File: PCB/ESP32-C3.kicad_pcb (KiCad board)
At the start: 2 copper layers, 28.3 x 28.5 mm, 50 parts, among them J1 HCZZ0039-3, J2 DPS_PPS_Right_Angle, SW1 TS-1187A-B-A-B, SW2 TS-1187A-B-A-B, U1 USB-C-16P-SMD, U2 BQ24073RGTR, U3 ESP32-C3, U4 DS8242-33SS3, Y1 40MHz_S3240000151040

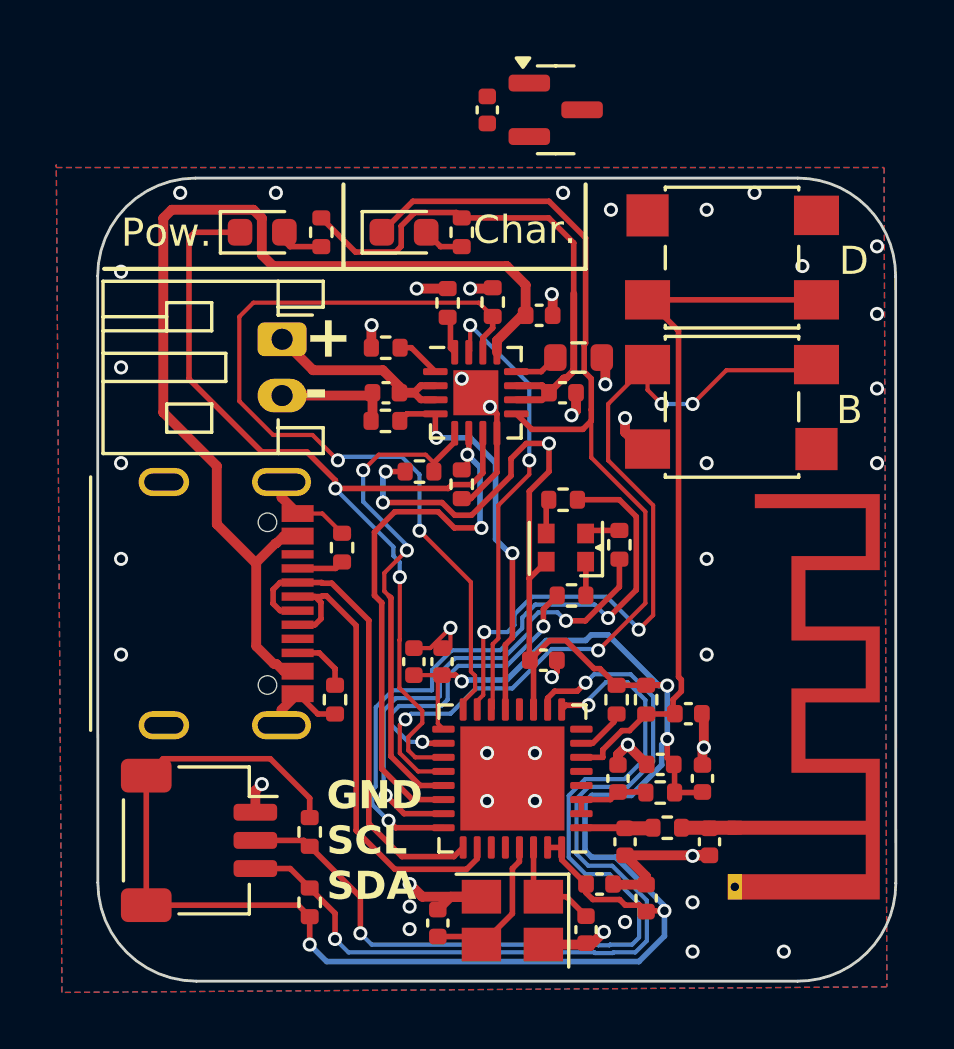
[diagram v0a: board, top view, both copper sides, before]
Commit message: LDO hinzugefügt
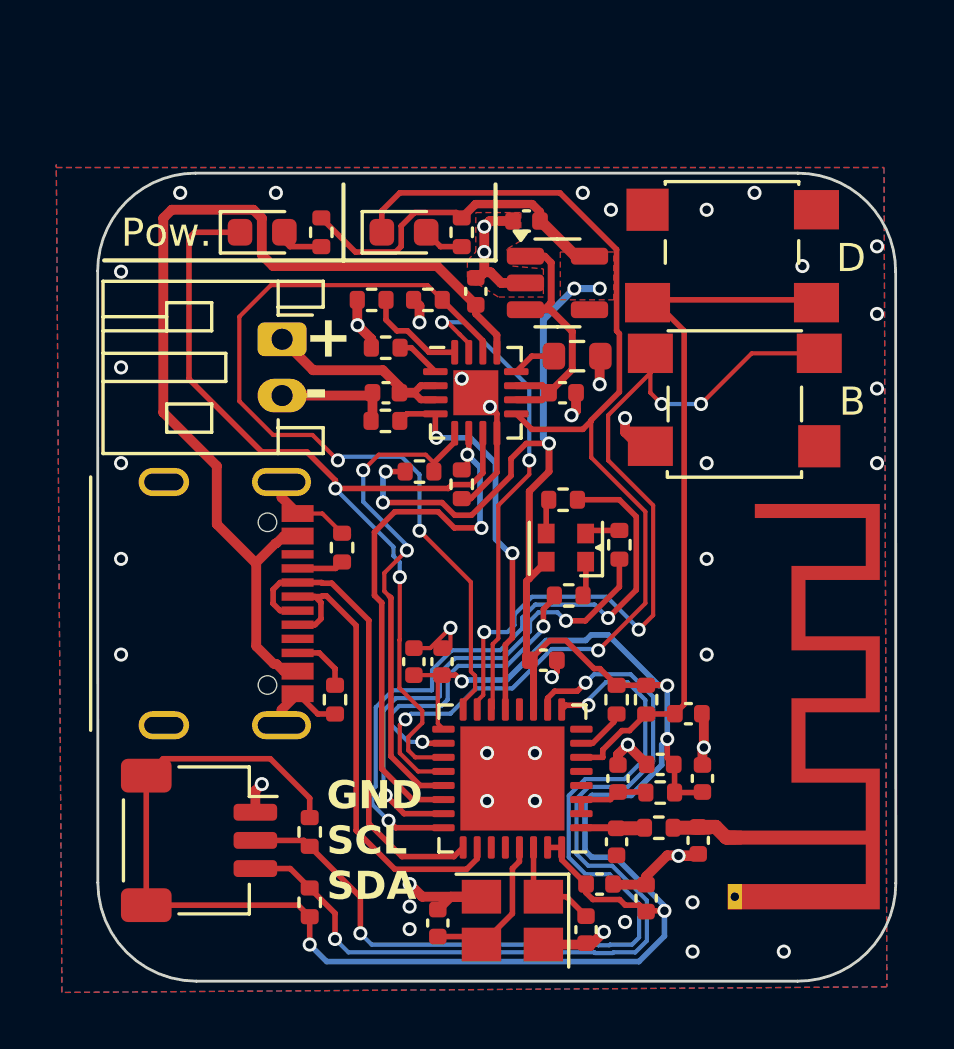
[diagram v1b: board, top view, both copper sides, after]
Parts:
- removed R19, R21: 100_0402, Resistor_SMD:R_0402_1005Metric
- removed U4: DS8242-33SS3, Package_TO_SOT_SMD:SOT-23
- added R12: 120_0402, Resistor_SMD:R_0402_1005Metric, F.Cu at (145.7, 82.6)
- added R13: 120_0402, Resistor_SMD:R_0402_1005Metric, F.Cu at (145.5, 79.2)
- added U5: WL9003S5-33, Package_TO_SOT_SMD:SOT-23-5, F.Cu at (145.3, 71.5)
- R14: value 100_0402 -> 120_0402
- moved C9 4.18 mm to (144.2, 69.3), turned to 180 degrees
- moved R18 2.70 mm to (138.7, 72.1), turned to 180 degrees
- moved R14 2.56 mm to (147.5, 80.8), turned to 90 degrees
- moved C19 2.41 mm to (142.4, 71.8), turned to 90 degrees
- moved R5 2.30 mm to (140.7, 72.1), turned to 0 degrees
- moved C3 0.40 mm to (150.3, 91.3)
- moved AE1 0.35 mm to (151.6, 91.2)
- moved C6 0.30 mm to (147.4, 91.3)
- moved L1 0.30 mm to (148.9, 90.8)
- moved SW1 0.20 mm to (151.5, 70.4)
- moved SW2 0.14 mm to (151.6, 75.8)
- moved R15 0.07 mm to (146.0, 74.1)
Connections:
- R14 pad 1: Grün -> Blau
- R14 pad 2: Net-(D1-GK) -> Net-(D1-BK)
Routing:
- net Net-(U5-EN): track 0.00 -> 10.3 mm
- net GND: track 42.8 -> 45.5 mm
- net VCC: track 38.1 -> 35.6 mm
- net Net-(U2-ISET): track 1.35 -> 3.63 mm
- net TD: track 16.1 -> 17.6 mm
- net NCHG: track 38.9 -> 40.4 mm
- net Net-(U3-GPIO9): track 27.9 -> 29.0 mm
- net Net-(AE1-A): track 1.91 -> 2.66 mm
- net Net-(U3-LNA_IN): track 2.56 -> 1.96 mm
- net +3.3V: track 111.4 -> 111.5 mm, vias 8 -> 10
- added copper zone on F.Cu, net +3.3V
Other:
- board size 28.3 x 28.5 mm -> 28.3 x 28.7 mm
- board text removed: "Char."

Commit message: Kleine Verbesserungen
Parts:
- D1: footprint LEDSMD:LED_0606_1432 -> LEDSMD:LED_0606_1432_correct
- turned D1 to 0 degrees
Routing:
- net Net-(D1-RK): track 1.20 -> 2.74 mm
- net Net-(D1-GK): track 1.24 -> 2.09 mm
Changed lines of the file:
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@@
 		)
 	)
-	(footprint "LEDSMD:LED_0606_1432"
+	(footprint "LEDSMD:LED_0606_1432_correct"
 		(layer "F.Cu")
-		(at 145.6 80.9 180)
+		(at 145.6 80.9)
 		(property "Reference" "D1"
-			(at 1.6 -0.02 -90)
+			(at 1.6 -0.02 90)
 			(unlocked yes)
 			(layer "F.SilkS")
@@
 		)
 		(property "Value" "XL-1615RGBC-RF"
-			(at 0 2.4 180)
+			(at 0 2.4 0)
 			(unlocked yes)
 			(layer "F.Fab")
@@
 			)
 		)
-		(property "Footprint" "LEDSMD:LED_0606_1432"
-			(at 0 0 180)
-			(unlocked yes)
+		(property "Footprint" "LEDSMD:LED_0606_1432_correct"
+			(at 0 0 360)
 			(layer "F.Fab")
 			(hide yes)
@@
 		)
 		(property "Datasheet" "https://datasheet.lcsc.com/lcsc/2211030000_XINGLIGHT-XL-1615RGBC-RF_C965840.pdf"
-			(at 0 0 180)
-			(unlocked yes)
+			(at 0 0 360)
 			(layer "F.Fab")
 			(hide yes)
@@
 		)
 		(property "Description" "Colorless transparence -30℃~+85℃ Positive post RGB 120° 0606  Light Emitting Diodes (LED) ROHS"
-			(at 0 0 180)
-			(unlocked yes)
+			(at 0 0 360)
 			(layer "F.Fab")
 			(hide yes)
@@
 		)
 		(property "LCSC" "C965840"
-			(at 0 0 180)
+			(at 0 0 360)
 			(layer "F.Fab")
 			(hide yes)
@@
 		)
 		(property "Price1000" "0.0106"
-			(at 0 0 180)
+			(at 0 0 0)
 			(unlocked yes)
 			(layer "F.Fab")
@@
 		)
 		(property "JLCPCB_CORRECTION" "0;0;180"
-			(at 0 0 180)
+			(at 0 0 0)
 			(unlocked yes)
 			(layer "F.Fab")
@@
 		(attr smd)
 		(fp_line
-			(start 1.3 0.9)
-			(end 1.3 -0.95)
+			(start -1.3 -1)
+			(end -0.525 -1)
 			(stroke
 				(width 0.12)
@@
 		)
 		(fp_line
-			(start -1.1 0)
-			(end -1.3 0.1)
+			(start -1.3 -0.1)
+			(end -1.1 0)
 			(stroke
 				(width 0.12)
@@
 		)
 		(fp_line
-			(start -1.3 -0.1)
-			(end -1.1 0)
+			(start -1.1 0)
+			(end -1.3 0.1)
 			(stroke
 				(width 0.12)
@@
 		)
 		(fp_line
-			(start -1.3 -1)
-			(end -0.525 -1)
+			(start 1.3 0.9)
+			(end 1.3 -0.95)
 			(stroke
 				(width 0.12)
@@
 			(layer "F.Fab")
 		)
+		(fp_text user "1"
+			(at -0.4 -0.2 0)
+			(unlocked yes)
+			(layer "F.SilkS")
+			(effects
+				(font
+					(size 0.5 0.5)
+					(thickness 0.125)
+				)
+				(justify left bottom)
+			)
+		)
 		(pad "1" smd rect
-			(at -0.7 -0.5 180)
+			(at -0.7 -0.5)
 			(size 0.6 0.7)
 			(layers "F.Cu" "F.Paste" "F.Mask")
@@
 		)
 		(pad "2" smd rect
-			(at 0.7 -0.5 180)
+			(at -0.7 0.5)
 			(size 0.6 0.7)
 			(layers "F.Cu" "F.Paste" "F.Mask")
@@
 		)
 		(pad "3" smd rect
-			(at -0.7 0.5 180)
+			(at 0.7 0.5)
 			(size 0.6 0.7)
 			(layers "F.Cu" "F.Paste" "F.Mask")
@@
 		)
 		(pad "4" smd rect
-			(at 0.7 0.5 180)
+			(at 0.7 -0.5)
 			(size 0.6 0.7)
 			(layers "F.Cu" "F.Paste" "F.Mask")
@@
 	(segment
 		(start 147.5 80.29)
-		(end 146.41 80.29)
+		(end 147.41 80.29)
 		(width 0.2)
 		(layer "F.Cu")
@@
 	)
 	(segment
-		(start 146.41 80.29)
-		(end 146.3 80.4)
+		(start 146.31 81.41)
+		(end 146.3 81.4)
+		(width 0.2)
+		(layer "F.Cu")
+		(net 32)
+	)
+	(segment
+		(start 147.41 80.29)
+		(end 146.3 81.4)
 		(width 0.2)
 		(layer "F.Cu")
@@
 	)
 	(segment
-		(start 144.9 80.4)
-		(end 144.9 79.29)
+		(start 146.41 80.29)
+		(end 146.3 80.4)
 		(width 0.2)
 		(layer "F.Cu")
@@
 	)
 	(segment
-		(start 146.31 81.41)
-		(end 146.3 81.4)
+		(start 144.99 79.2)
+		(end 145.1 79.2)
+		(width 0.2)
+		(layer "F.Cu")
+		(net 36)
+	)
+	(segment
+		(start 145.1 79.2)
+		(end 146.3 80.4)
+		(width 0.2)
+		(layer "F.Cu")
+		(net 36)
+	)
+	(segment
+		(start 145.6 81.99)
+		(end 145.6 81.1)
+		(width 0.2)
+		(layer "F.Cu")
+		(net 37)
+	)
+	(segment
+		(start 145.6 81.1)
+		(end 144.9 80.4)
 		(width 0.2)
 		(layer "F.Cu")
@@
 	)
 	(segment
-		(start 146.31 82.6)
-		(end 146.31 81.41)
+		(start 146.21 82.6)
+		(end 145.6 81.99)
 		(width 0.2)
 		(layer "F.Cu")
